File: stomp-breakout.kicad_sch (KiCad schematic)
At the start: 12 parts, among them J1 Stomp_Connector, J2 OUT, J3 IN, J4 Power_SIDE, J5 Power_TOP, J6 GND, J7 GND

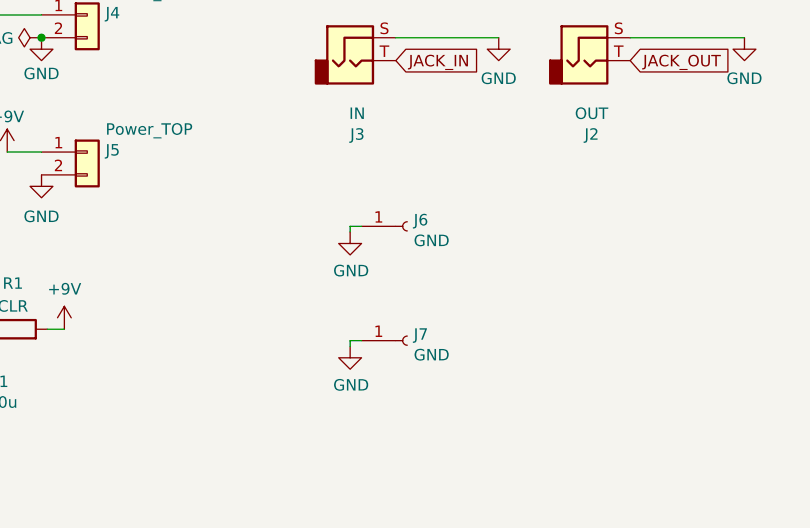
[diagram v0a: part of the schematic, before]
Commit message: updated to KiCad 6.0
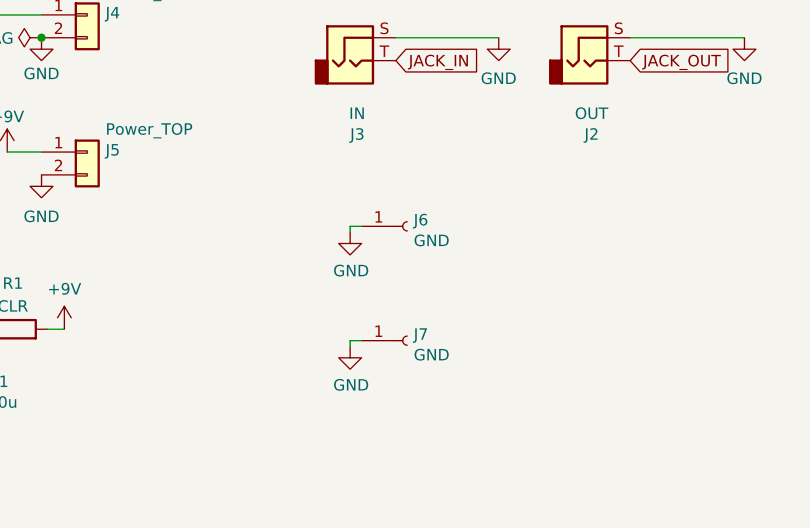
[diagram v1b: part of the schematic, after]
